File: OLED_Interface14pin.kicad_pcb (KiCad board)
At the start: 2 copper layers, 7.6 x 8.9 mm, 13 parts, among them J1 INT, J2 OLED

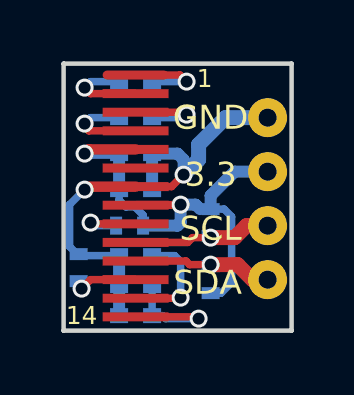
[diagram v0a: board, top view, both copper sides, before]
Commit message: Adding capacitor to RST for proper init
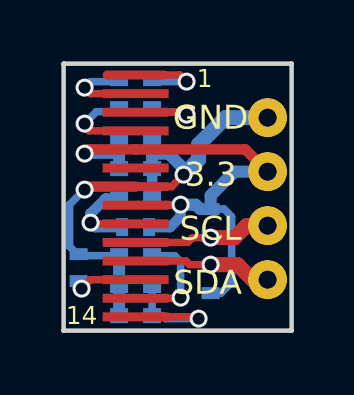
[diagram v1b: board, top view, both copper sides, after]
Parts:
- added C8: 1uf, Capacitors_SMD:C_0402_NoSilk, B.Cu at (170.0, 104.6)
- moved C1 0.70 mm to (170.0, 103.6)
- moved C3 0.50 mm to (170.0, 102.6)
- moved C4 0.30 mm to (170.0, 101.6)
- moved R4 0.21 mm to (170.0, 105.5)
- moved C6 0.10 mm to (170.0, 100.6)
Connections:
- net Net-(J1-Pad3) renamed /SCL
- net Net-(J1-Pad4) renamed /SDA
- net Net-(J2-Pad9) renamed /RST
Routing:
- net +3V3: track 19.4 -> 21.8 mm
- net /RST: track 2.41 -> 4.23 mm
- net GND: track 16.0 -> 16.6 mm
